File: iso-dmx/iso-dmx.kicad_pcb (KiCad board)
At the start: 2 copper layers, 19 x 16.5 mm, 8 parts, among them J1 Conn_01x06, J2 Conn_01x06, U1 ISO1432BDW

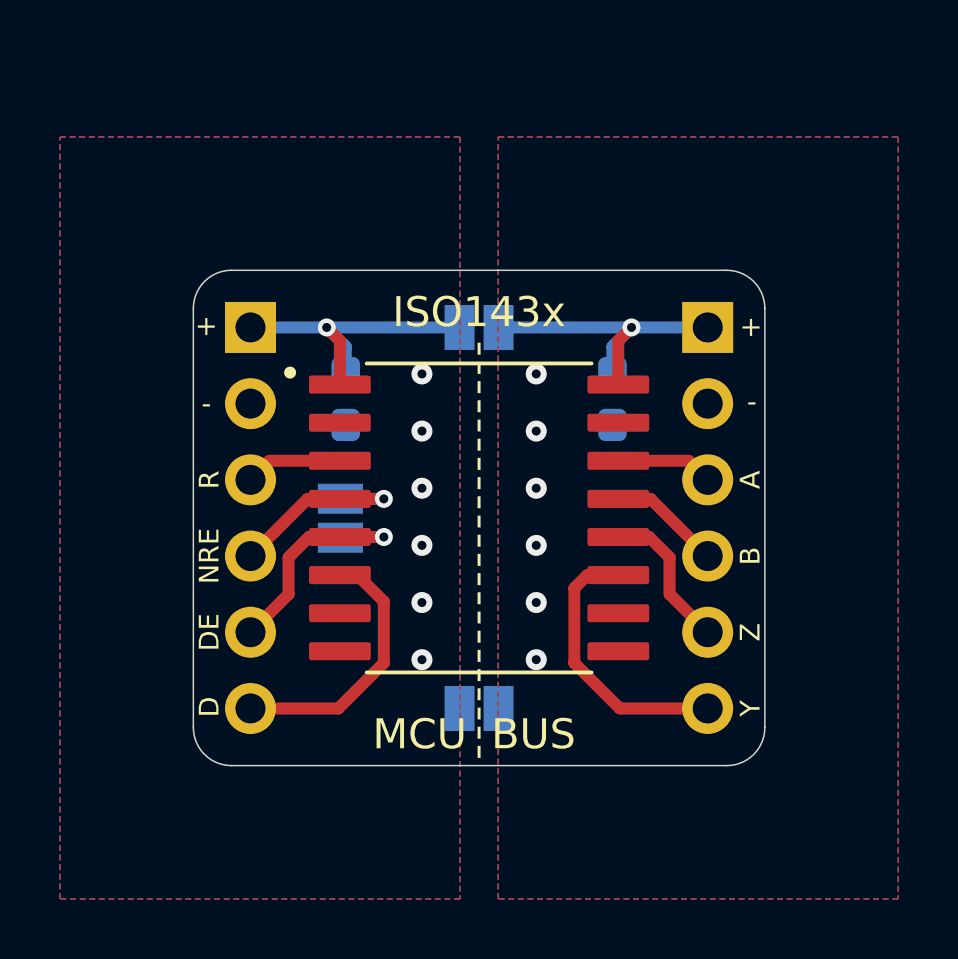
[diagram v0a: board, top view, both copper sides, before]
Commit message: Added isolated voltage regulator to RS485 board
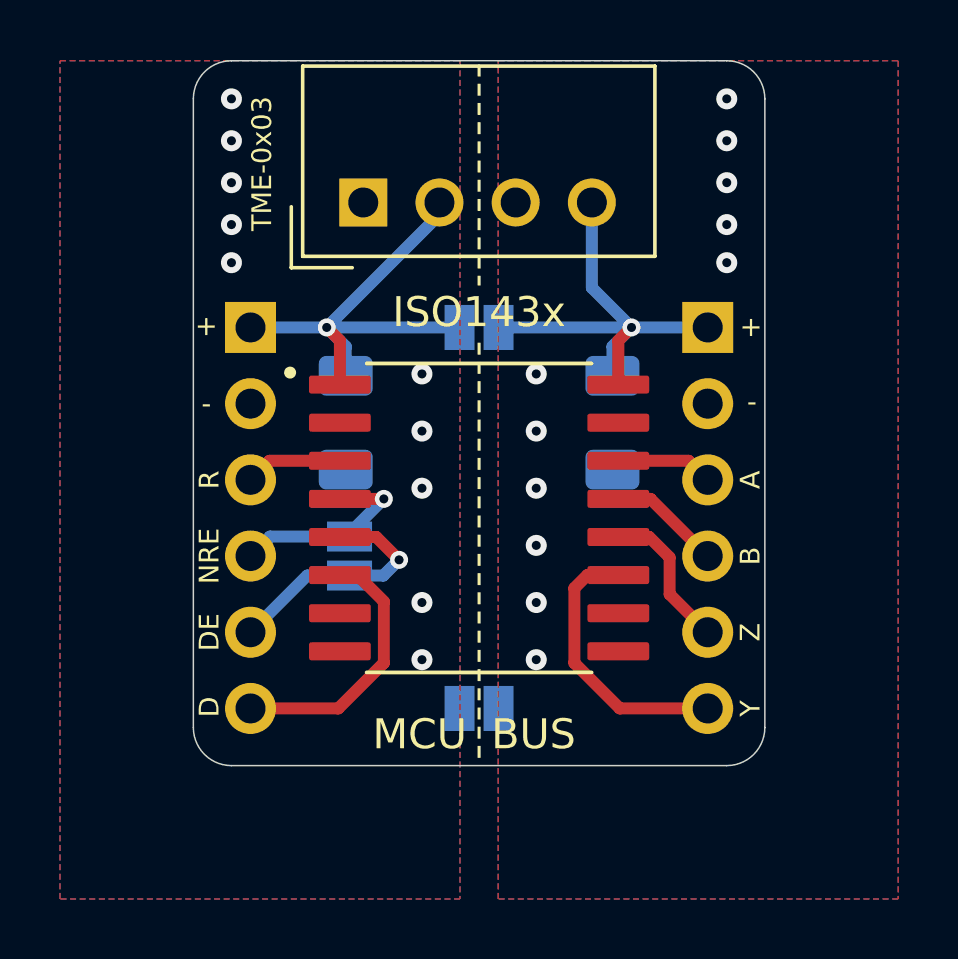
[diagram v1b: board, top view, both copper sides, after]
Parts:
- added U2: TME-0305S, Converter_DCDC:Converter_DCDC_TRACO_TME_03xxS_05xxS_12xxS_Single_THT, F.Cu at (80.0, 46.6)
- C1, C2: footprint Capacitor_SMD:C_0603_1608Metric_Pad1.08x0.95mm_HandSolder -> Capacitor_SMD:C_1206_3216Metric_Pad1.33x1.80mm_HandSolder
- moved JP1 1.30 mm to (79.5, 58.4)
- moved C1 0.79 mm to (88.3, 54.0)
- moved C2 0.79 mm to (79.4, 54.0)
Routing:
- net VCC: track 10.8 -> 16.6 mm
- net VCC2: track 10.8 -> 15.6 mm
- net GND2: vias 6 -> 11
- net GND1: vias 6 -> 10
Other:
- board size 19 x 16.5 mm -> 19 x 23.5 mm
- board text added: "TME-0x03"
